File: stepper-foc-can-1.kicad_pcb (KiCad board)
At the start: 4 copper layers, 42 x 48 mm, 87 parts, among them J1 TC2030, J2 Conn_01x02, J3 Conn_01x04_Pin, J4 Conn_01x02, J5 Conn_01x02, M1 Stepper_Motor_bipolar, SW1 SW_Push, SW2 SW_Push, SW3 SW_Push, SW4 SW_Push, U1 STM32G474RBTx, U2 MX25947, U3 TPS62933, U4 TCAN3413, U5 AS5047P, U6 DRV8874, U7 INA241A3IDDF, U8 DRV8874, U9 INA241A3IDDF, Y1 Crystal_GND24

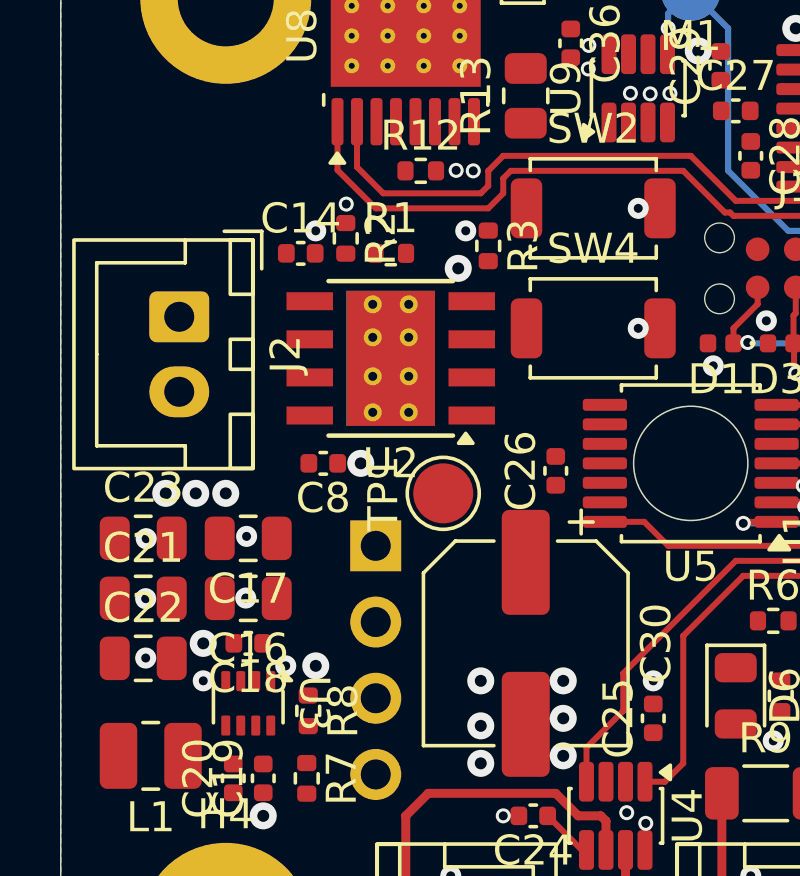
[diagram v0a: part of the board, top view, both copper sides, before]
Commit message: pcb: add efuse routing
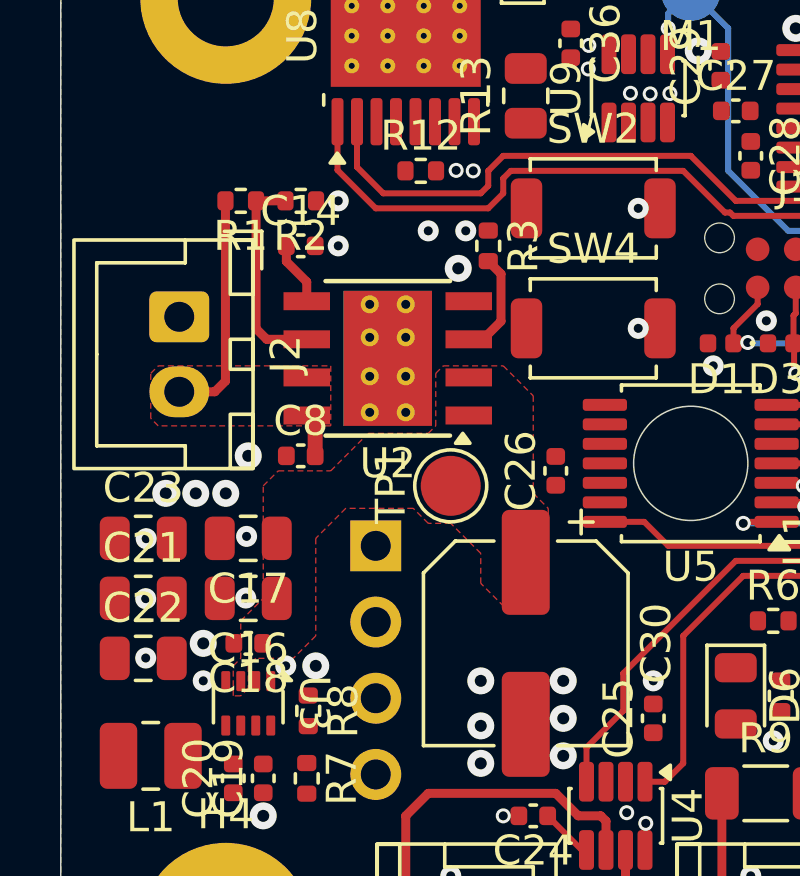
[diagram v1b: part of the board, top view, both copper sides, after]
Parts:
- moved R1 5.30 mm to (129.0, 72.2), turned to 180 degrees
- moved R2 1.95 mm to (131.0, 72.2), turned to 180 degrees
- moved C8 0.79 mm to (131.0, 80.8), turned to 0 degrees
- moved TP1 0.35 mm to (136.0, 81.8)
- moved C14 0.25 mm to (131.0, 73.8)
- moved U2 0.10 mm to (133.9, 77.5)
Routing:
- net VIN: track 0.00 -> 9.29 mm
- net Net-(U2-EN/UVLO): track 0.00 -> 7.18 mm
- net Net-(U2-ILIMIT): track 0.00 -> 3.50 mm
- net Net-(U2-DVDT): track 0.00 -> 2.13 mm
- net GND: vias 88 -> 89
- added copper zone on F.Cu, net +12V
- added copper zone on F.Cu, net VIN

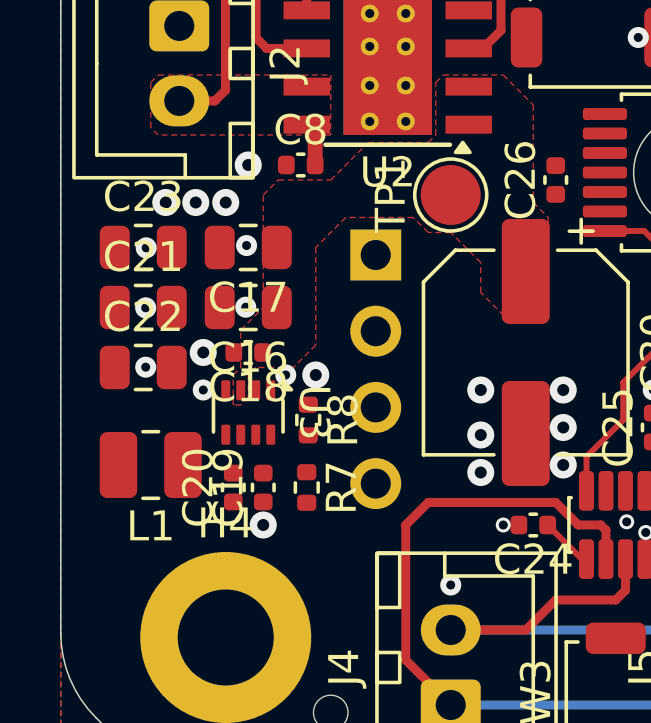
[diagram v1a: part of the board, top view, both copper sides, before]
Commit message: pcb: add smps routing
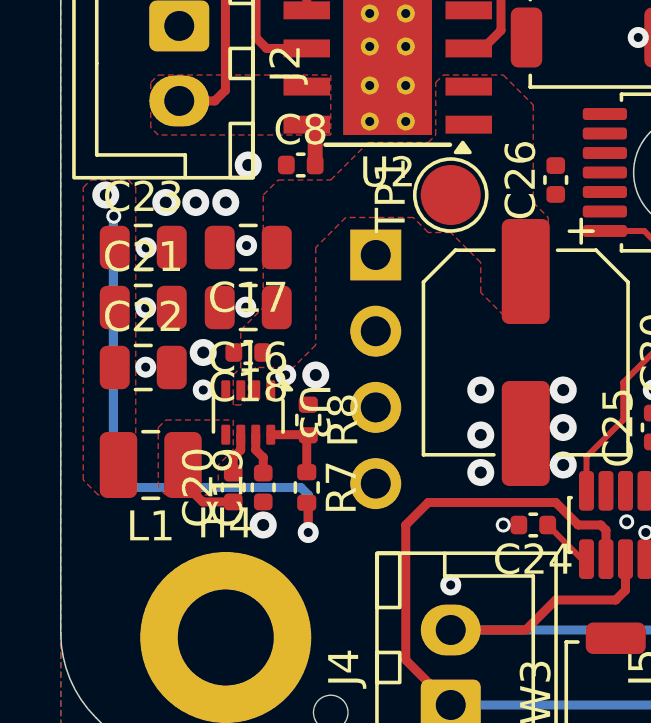
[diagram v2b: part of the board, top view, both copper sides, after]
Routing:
- net +3V3: track 5.71 -> 23.2 mm, vias 0 -> 3
- net Net-(U3-SW): track 0.00 -> 2.52 mm
- net Net-(U3-FB): track 0.00 -> 2.51 mm
- net Net-(U3-SS): track 0.00 -> 1.38 mm
- net Net-(U3-BST): track 0.00 -> 1.38 mm
- added copper zone on F.Cu, net +3V3
- added copper zone on F.Cu, net Net-(U3-SW)
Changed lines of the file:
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@@
+	)
+	(segment
+		(start 131.25 93)
+		(end 131.25 92.06)
+		(width 0.3)
+		(layer "F.Cu")
+		(net "+3V3")
 	)
 	(segment
@@
 	)
 	(segment
+		(start 131.25 92.06)
+		(end 131.2 92.01)
+		(width 0.3)
+		(layer "F.Cu")
+		(net "+3V3")
+	)
+	(segment
 		(start 151 74.264565)
 		(end 151 74.675)
@@
 		(width 0.2)
 		(layer "F.Cu")
+		(net "+3V3")
+	)
+	(via
+		(at 124.5 81.75)
+		(size 0.9)
+		(drill 0.4)
+		(layers "F.Cu" "B.Cu")
+		(free yes)
+		(net "+3V3")
+	)
+	(via
+		(at 124.768254 82.457616)
+		(size 0.5)
+		(drill 0.3)
+		(layers "F.Cu" "B.Cu")
+		(net "+3V3")
+	)
+	(via
+		(at 131.25 93)
+		(size 0.7)
+		(drill 0.3)
+		(layers "F.Cu" "B.Cu")
+		(net "+3V3")
+	)
+	(segment
+		(start 124.75 82.47587)
+		(end 124.75 90.75)
+		(width 0.3)
+		(layer "B.Cu")
+		(net "+3V3")
+	)
+	(segment
+		(start 131.25 91.75)
+		(end 131.25 93)
+		(width 0.3)
+		(layer "B.Cu")
+		(net "+3V3")
+	)
+	(segment
+		(start 124.75 90.75)
+		(end 125.5 91.5)
+		(width 0.3)
+		(layer "B.Cu")
+		(net "+3V3")
+	)
+	(segment
+		(start 131 91.5)
+		(end 131.25 91.75)
+		(width 0.3)
+		(layer "B.Cu")
+		(net "+3V3")
+	)
+	(segment
+		(start 125.5 91.5)
+		(end 131 91.5)
+		(width 0.3)
+		(layer "B.Cu")
+		(net "+3V3")
+	)
+	(segment
+		(start 124.768254 82.457616)
+		(end 124.75 82.47587)
+		(width 0.3)
+		(layer "B.Cu")
 		(net "+3V3")
 	)
@@
 		(layer "F.Cu")
 		(net "VIN")
+	)
+	(segment
+		(start 127.73 91.98)
+		(end 128.75 91.98)
+		(width 0.3)
+		(layer "F.Cu")
+		(net "Net-(U3-SW)")
+	)
+	(segment
+		(start 127.075 90.75)
+		(end 127.075 91.325)
+		(width 0.3)
+		(layer "F.Cu")
+		(net "Net-(U3-SW)")
+	)
+	(segment
+		(start 127.075 91.325)
+		(end 127.73 91.98)
+		(width 0.3)
+		(layer "F.Cu")
+		(net "Net-(U3-SW)")
 	)
 	(segment
@@
 	)
 	(segment
+		(start 129 90.25)
+		(end 129 89.74)
+		(width 0.3)
+		(layer "F.Cu")
+		(net "Net-(U3-BST)")
+	)
+	(segment
+		(start 128.75 91.02)
+		(end 128.75 90.5)
+		(width 0.3)
+		(layer "F.Cu")
+		(net "Net-(U3-BST)")
+	)
+	(segment
+		(start 128.75 90.5)
+		(end 129 90.25)
+		(width 0.3)
+		(layer "F.Cu")
+		(net "Net-(U3-BST)")
+	)
+	(segment
+		(start 129.5 90.25)
+		(end 129.5 89.74)
+		(width 0.3)
+		(layer "F.Cu")
+		(net "Net-(U3-SS)")
+	)
+	(segment
+		(start 129.75 91.02)
+		(end 129.75 90.5)
+		(width 0.3)
+		(layer "F.Cu")
+		(net "Net-(U3-SS)")
+	)
+	(segment
+		(start 129.75 90.5)
+		(end 129.5 90.25)
+		(width 0.3)
+		(layer "F.Cu")
+		(net "Net-(U3-SS)")
+	)
+	(segment
+		(start 131.2 90.99)
+		(end 131.2 89.81)
+		(width 0.3)
+		(layer "F.Cu")
+		(net "Net-(U3-FB)")
+	)
+	(segment
+		(start 131.2 89.81)
+		(end 131.25 89.76)
+		(width 0.3)
+		(layer "F.Cu")
+		(net "Net-(U3-FB)")
+	)
+	(segment
+		(start 130 89.74)
+		(end 131.23 89.74)
+		(width 0.3)
+		(layer "F.Cu")
+		(net "Net-(U3-FB)")
+	)
+	(segment
+		(start 131.23 89.74)
+		(end 131.25 89.76)
+		(width 0.3)
+		(layer "F.Cu")
+		(net "Net-(U3-FB)")
+	)
+	(segment
 		(start 147.9625 92)
 		(end 147.9625 93.7125)
@@
 		(layer "F.Cu")
 		(net "Net-(U8-CPL)")
+	)
+	(zone
+		(net "+3V3")
+		(layer "F.Cu")
+		(hatch edge 0.5)
+		(priority 4)
+		(connect_pads yes
+			(clearance 0.2)
+		)
+		(min_thickness 0.15)
+		(fill yes
+			(thermal_gap 0.25)
+			(thermal_bridge_width 0.35)
+			(island_removal_mode 0)
+		)
+		(polygon
+			(pts
+				(xy 125.25 91.75) (xy 124.25 91.75) (xy 123.75 91.25) (xy 123.75 81.5) (xy 124 81.25) (xy 125.25 81.25)
+				(xy 125.5 81.5) (xy 125.5 91.5)
+			)
+		)
 	)
 	(zone
@@
 	)
 	(zone
+		(net "Net-(U3-SW)")
+		(layer "F.Cu")
+		(hatch edge 0.5)
+		(priority 3)
+		(connect_pads yes
+			(clearance 0.2)
+		)
+		(min_thickness 0.15)
+		(fill yes
+			(thermal_gap 0.5)
+			(thermal_bridge_width 0.5)
+			(island_removal_mode 0)
+		)
+		(polygon
+			(pts
+				(xy 128.75 89.25) (xy 128.75 90.25) (xy 128.25 90.75) (xy 128.25 91.5) (xy 128 91.75) (xy 126.5 91.75)
+				(xy 126.25 91.5) (xy 126.25 89.5) (xy 126.5 89.25)
+			)
+		)
+	)
+	(zone
 		(layer "F.Cu")
 		(hatch edge 0.5)
@@
 		(min_thickness 0.15)
 		(fill yes
-			(thermal_gap 0.35)
+			(thermal_gap 0.25)
 			(thermal_bridge_width 0.35)
 			(island_removal_mode 0)

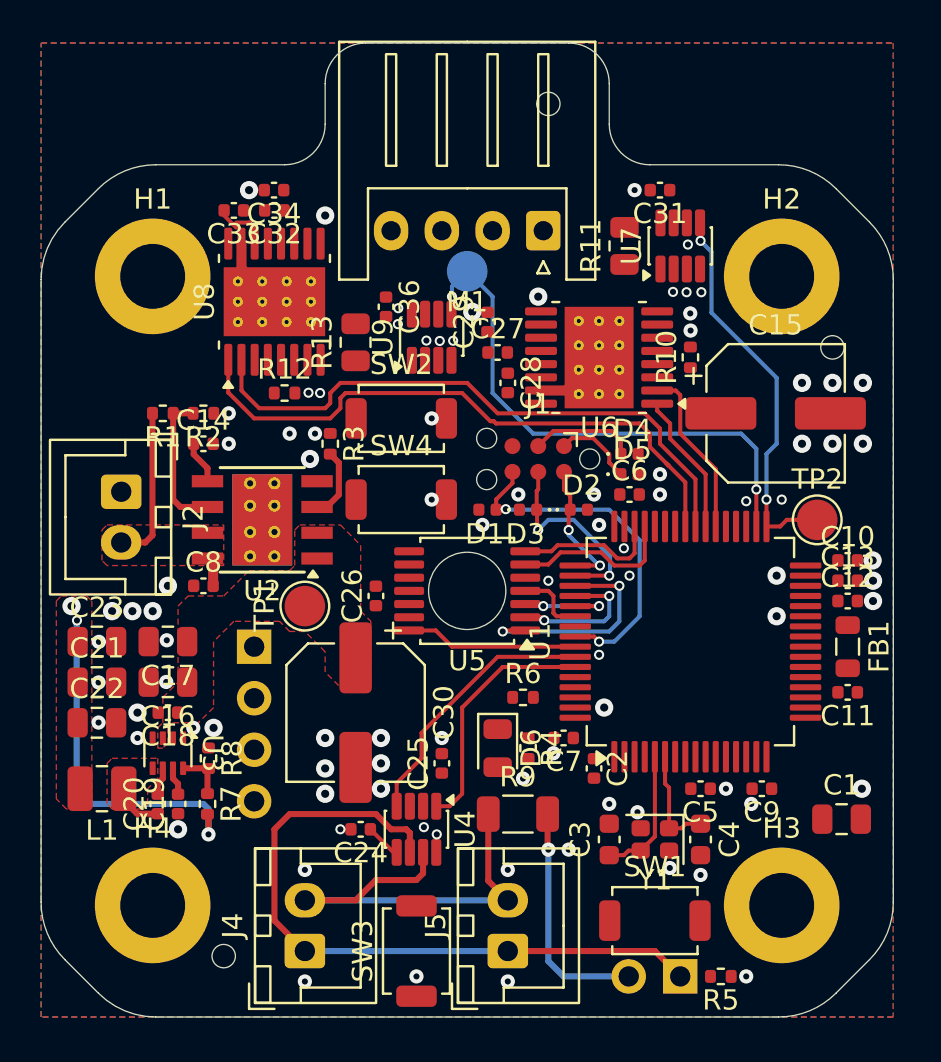
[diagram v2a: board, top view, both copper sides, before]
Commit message: pcb: add +12v and drvs routing
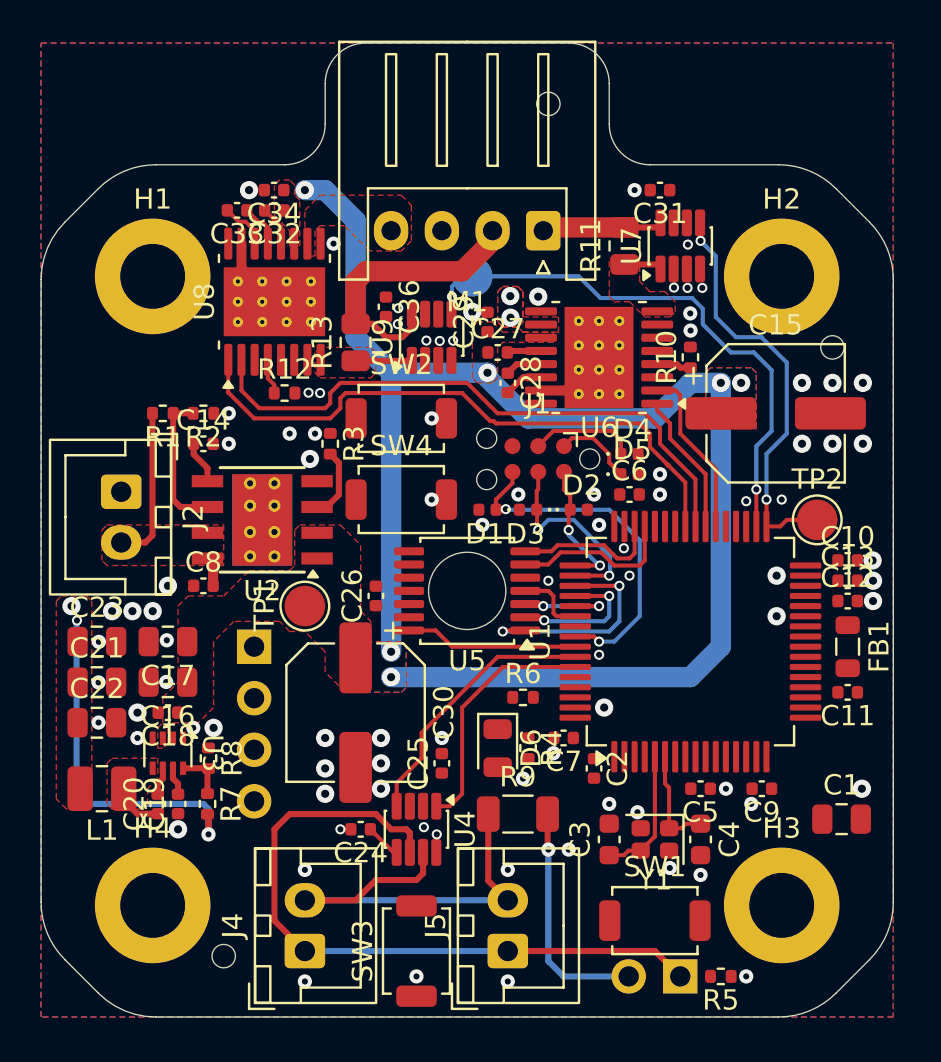
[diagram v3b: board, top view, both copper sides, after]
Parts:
- moved TP3 0.35 mm to (144.2, 65.5)
- moved C33 0.16 mm to (132.7, 62.2)
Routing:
- net +12V: track 0.00 -> 73.0 mm, vias 0 -> 6
- net /H-bridge A/OUT-: track 0.00 -> 18.4 mm, vias 0 -> 2
- net /H-bridge B/OUT+: track 0.00 -> 14.1 mm
- net /H-bridge A/OUT+: track 0.00 -> 6.00 mm
- net Net-(U8-OUT1): track 0.00 -> 2.79 mm
- net Net-(U8-CPH): track 0.00 -> 2.18 mm
- net Net-(U8-VCP): track 0.00 -> 1.97 mm
- net Net-(U6-CPL): track 0.00 -> 1.95 mm
- net Net-(U6-OUT1): track 0.00 -> 1.93 mm
- net Net-(U6-CPH): track 0.00 -> 1.82 mm
- net /~{FAULT_B}: track 0.00 -> 1.77 mm
- net /~{FAULT_A}: track 0.00 -> 1.71 mm
- net Net-(U6-VCP): track 0.00 -> 1.69 mm
- net /SNS_A: track 19.4 -> 20.5 mm
- net /SNS_B: track 26.9 -> 27.7 mm
- added copper zone on B.Cu, net +12V
- added copper zone on B.Cu, net /H-bridge A/OUT-
- added copper zone on F.Cu, net /H-bridge A/OUT-
- added copper zone on F.Cu, net /H-bridge B/OUT-
- added copper zone on F.Cu, net Net-(U6-OUT1)
- added copper zone on F.Cu, net Net-(U8-OUT1)

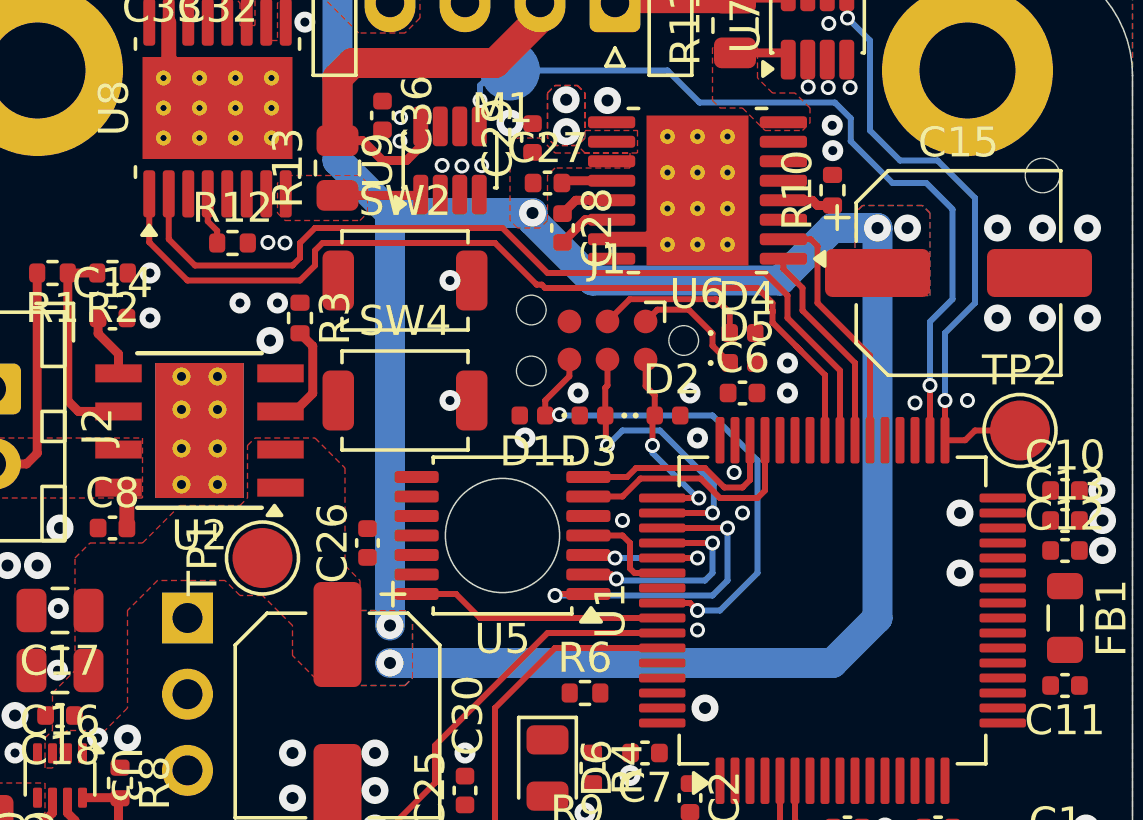
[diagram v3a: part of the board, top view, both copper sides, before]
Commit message: pcb: add drv sleep/fault routing
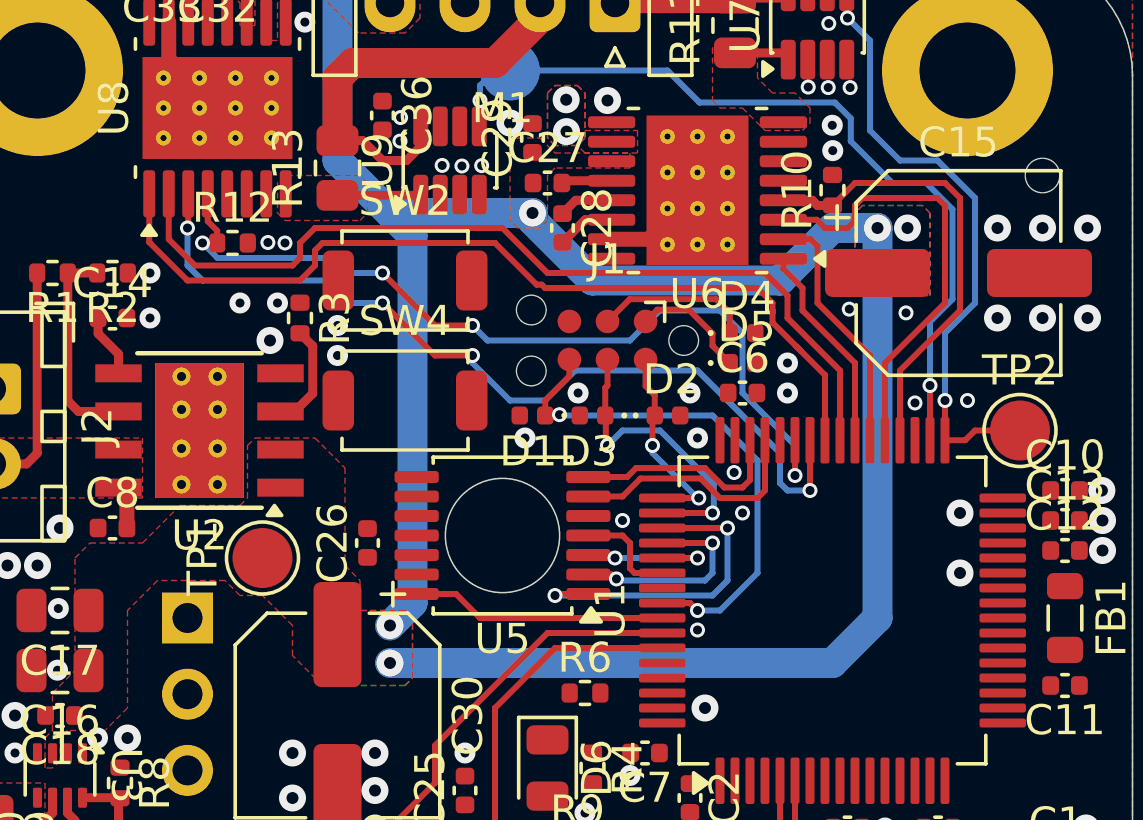
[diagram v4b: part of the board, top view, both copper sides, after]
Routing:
- net /~{SLEEP_B}: track 0.00 -> 29.5 mm, vias 0 -> 4
- net /~{FAULT_B}: track 1.77 -> 29.0 mm, vias 0 -> 4
- net /~{SLEEP_A}: track 0.00 -> 15.0 mm
- net /~{FAULT_A}: track 1.71 -> 15.4 mm
- net +12V: track 73.0 -> 73.6 mm
- net GND: vias 89 -> 91
